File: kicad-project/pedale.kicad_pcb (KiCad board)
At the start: 2 copper layers, 118 x 73 mm, 32 parts, among them IC1 TLV76150DCYR, IC2 TLV76150DCYR, IC3 TLV76150DCYR, IC4 TLV76150DCYR, IC5 TLV76150DCYR

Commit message: Fixed 3 drc errors
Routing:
- net Net-(J14-pta8): track 30.9 -> 32.4 mm
- net Net-(J14-pta13): track 23.8 -> 25.3 mm
- net Net-(J14-pta9): track 38.1 -> 39.5 mm

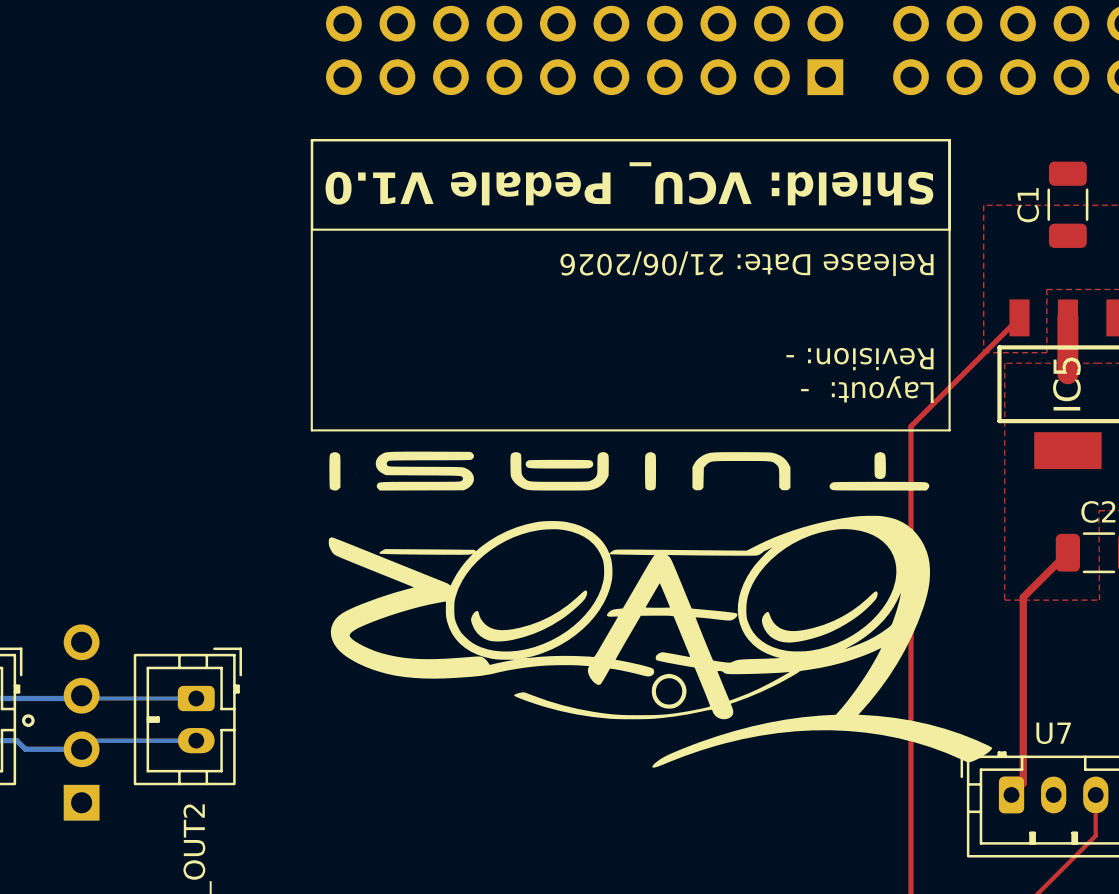
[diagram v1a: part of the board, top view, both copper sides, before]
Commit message: Fix one DRC warning for silkscreen
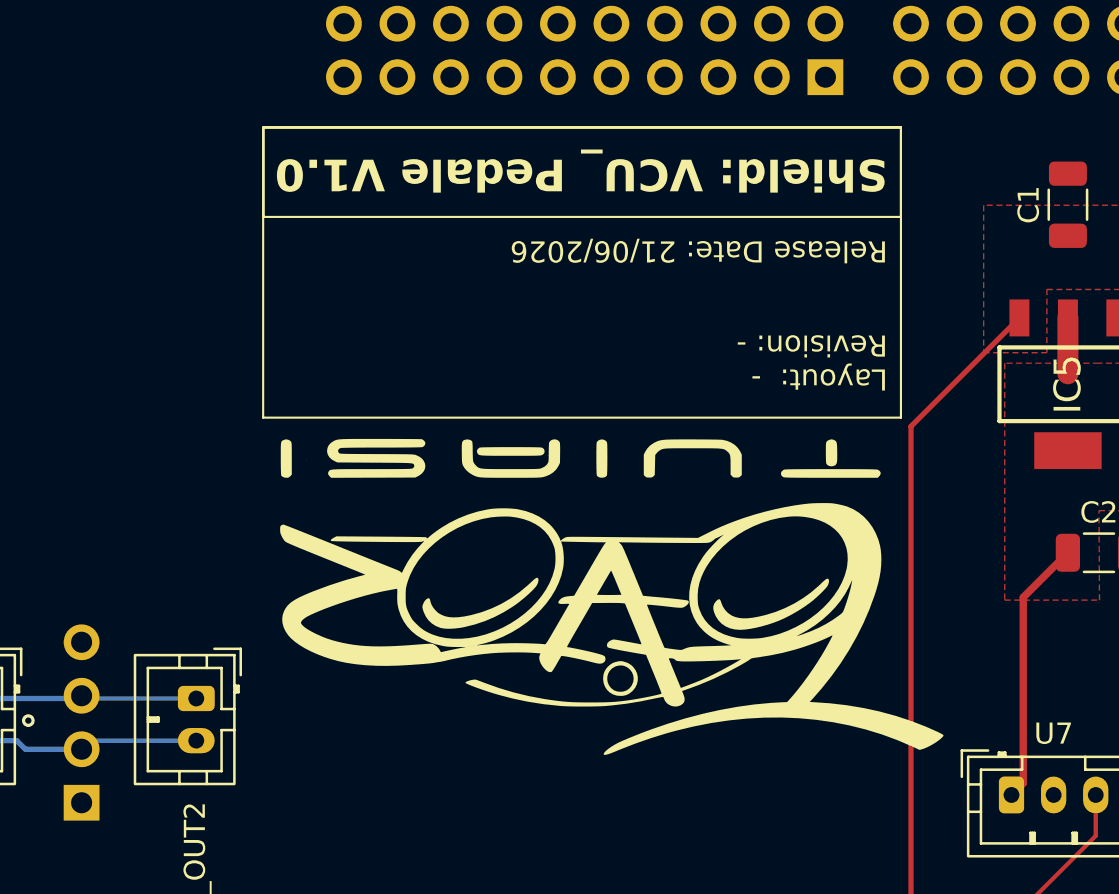
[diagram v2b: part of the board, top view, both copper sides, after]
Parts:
- moved G*** 2.39 mm to (56.5, 61.9)
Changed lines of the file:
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@@
 	(footprint "LOGO"
 		(layer "F.Cu")
-		(at 58.76 62.48 180)
+		(at 56.45 61.875 180)
 		(property "Reference" "G***"
 			(at 0 0 0)
@@
 		)
 		(property "Value" "1μF"
-			(at -0.1 -3.5 90)
+			(at -0.070001 -3.56 90)
 			(layer "F.Fab")
 			(effects
@@
 	(gr_poly
 		(pts
-			(xy 72.491955 40.19) (xy 72.491956 53.970001) (xy 42.21 53.970001) (xy 42.21 40.19)
+			(xy 70.181955 39.585) (xy 70.181956 53.365001) (xy 39.9 53.365001) (xy 39.9 39.585)
 		)
 		(stroke
@@
 	)
 	(gr_rect
-		(start 42.228045 40.19)
-		(end 72.491955 44.44)
+		(start 39.918045 39.585)
+		(end 70.181955 43.835)
 		(stroke
 			(width 0.1)
@@
 	)
 	(gr_text "Release Date: 21/06/2026"
-		(at 71.865158 45.48 180)
+		(at 69.555158 44.875 180)
 		(layer "F.SilkS")
 		(effects
@@
 	)
 	(gr_text "Layout:  -\nRevision: -"
-		(at 71.865159 49.95 180)
+		(at 69.555159 49.345 180)
 		(layer "F.SilkS")
 		(effects
@@
 	)
 	(gr_text "Shield: VCU_ Pedale V1.0"
-		(at 71.865159 41.54 180)
+		(at 69.555159 40.935 180)
 		(layer "F.SilkS")
 		(effects

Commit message: GBR added
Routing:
- net /CAN_P: track 10.5 -> 12.0 mm
- net /CAN_N: track 11.1 -> 12.4 mm
- net GND: vias 2 -> 1
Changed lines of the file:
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@@
 			(usegerberextensions no)
 			(usegerberattributes yes)
-			(usegerberadvancedattributes yes)
-			(creategerberjobfile yes)
+			(usegerberadvancedattributes no)
+			(creategerberjobfile no)
 			(dashed_line_dash_ratio 12)
 			(dashed_line_gap_ratio 3)
@@
 			(outputformat 1)
 			(mirror no)
-			(drillshape 1)
+			(drillshape 0)
 			(scaleselection 1)
-			(outputdirectory "")
+			(outputdirectory "GBR_29062026/")
 		)
 	)
@@
 	)
 	(via
-		(at 28.75 67.75)
-		(size 0.6)
-		(drill 0.3)
-		(layers "F.Cu" "B.Cu")
-		(free yes)
-		(capping no)
-		(covering
-			(front no)
-			(back no)
-		)
-		(plugging
-			(front no)
-			(back no)
-		)
-		(filling no)
-		(net "GND")
-	)
-	(via
 		(at 116.79 41.53)
 		(size 1.2)
@@
 	)
 	(segment
-		(start 31.410001 66.700001)
-		(end 31.28 66.57)
+		(start 35.855001 67.57)
+		(end 32.28 67.57)
 		(width 0.2)
 		(layer "B.Cu")
@@
 	(segment
 		(start 36.725 66.700001)
-		(end 31.410001 66.700001)
+		(end 35.855001 67.57)
 		(width 0.2)
 		(layer "B.Cu")
@@
 	)
 	(segment
-		(start 31.15 66.7)
-		(end 26.3 66.7)
-		(width 0.25)
+		(start 32.28 67.57)
+		(end 31.28 66.57)
+		(width 0.2)
 		(layer "B.Cu")
 		(net "/CAN_P")
@@
 	(segment
 		(start 31.28 66.57)
-		(end 31.15 66.7)
-		(width 0.25)
+		(end 31.13 66.57)
+		(width 0.2)
 		(layer "B.Cu")
 		(net "/CAN_P")
 	)
 	(segment
-		(start 36.725 68.700002)
-		(end 31.689998 68.700002)
+		(start 30.13 67.57)
+		(end 27.17 67.57)
 		(width 0.2)
 		(layer "B.Cu")
-		(net "/CAN_N")
+		(net "/CAN_P")
 	)
 	(segment
-		(start 28.2 68.7)
-		(end 26.3 68.7)
-		(width 0.25)
+		(start 27.17 67.57)
+		(end 26.3 66.7)
+		(width 0.2)
+		(layer "B.Cu")
+		(net "/CAN_P")
+	)
+	(segment
+		(start 31.13 66.57)
+		(end 30.13 67.57)
+		(width 0.2)
+		(layer "B.Cu")
+		(net "/CAN_P")
+	)
+	(segment
+		(start 35.8 67.97)
+		(end 32.3 67.97)
+		(width 0.2)
 		(layer "B.Cu")
 		(net "/CAN_N")
@@
 	)
 	(segment
+		(start 27.25 67.97)
+		(end 26.52 68.7)
+		(width 0.2)
+		(layer "B.Cu")
+		(net "/CAN_N")
+	)
+	(segment
 		(start 26.3 68.7)
 		(end 26.3 68.975)
@@
 	)
 	(segment
-		(start 28.61 69.11)
-		(end 28.2 68.7)
-		(width 0.25)
+		(start 31.28 68.99)
+		(end 31.28 69.11)
+		(width 0.2)
 		(layer "B.Cu")
 		(net "/CAN_N")
@@
 	(segment
 		(start 31.28 69.11)
-		(end 28.61 69.11)
-		(width 0.25)
+		(end 30.14 67.97)
+		(width 0.2)
 		(layer "B.Cu")
 		(net "/CAN_N")
 	)
 	(segment
-		(start 31.689998 68.700002)
-		(end 31.28 69.11)
+		(start 26.52 68.7)
+		(end 26.3 68.7)
+		(width 0.2)
+		(layer "B.Cu")
+		(net "/CAN_N")
+	)
+	(segment
+		(start 32.3 67.97)
+		(end 31.28 68.99)
+		(width 0.2)
+		(layer "B.Cu")
+		(net "/CAN_N")
+	)
+	(segment
+		(start 30.14 67.97)
+		(end 27.25 67.97)
+		(width 0.2)
+		(layer "B.Cu")
+		(net "/CAN_N")
+	)
+	(segment
+		(start 36.725 68.700002)
+		(end 36.530002 68.700002)
+		(width 0.2)
+		(layer "B.Cu")
+		(net "/CAN_N")
+	)
+	(segment
+		(start 36.530002 68.700002)
+		(end 35.8 67.97)
 		(width 0.2)
 		(layer "B.Cu")
@@
 		(hatch edge 0.5)
 		(priority 1)
-		(connect_pads
+		(connect_pads yes
 			(clearance 0.5)
 		)
@@
 			(thermal_gap 0.5)
 			(thermal_bridge_width 0.5)
+			(smoothing fillet)
+			(radius 2)
 			(island_removal_mode 0)
 		)
@@
 		(hatch edge 0.5)
 		(priority 2)
-		(connect_pads
+		(connect_pads yes
 			(clearance 0.5)
 		)
@@
 	)
 	(zone
-		(layers "F.Cu" "B.Cu")
-		(name "Supply GND")
-		(hatch edge 0.5)
-		(connect_pads
-			(clearance 0)
-		)
-		(min_thickness 0.25)
-		(keepout
-			(tracks allowed)
-			(vias allowed)
-			(pads allowed)
-			(copperpour not_allowed)
-			(footprints allowed)
-		)
-		(placement
-			(enabled no)
-			(sheetname "/")
-		)
-		(fill
-			(thermal_gap 0.5)
-			(thermal_bridge_width 0.5)
-			(island_removal_mode 0)
-		)
-		(polygon
-			(pts
-				(xy 123.38 40.8) (xy 123.42 43.9) (xy 128.141311 43.872342) (xy 128.123253 40.789744)
-			)
-		)
-	)
-	(zone
-		(layers "F.Cu" "B.Cu")
-		(name "Supply GND")
-		(hatch edge 0.5)
-		(connect_pads
-			(clearance 0)
-		)
-		(min_thickness 0.25)
-		(keepout
-			(tracks allowed)
-			(vias allowed)
-			(pads allowed)
-			(copperpour not_allowed)
-			(footprints allowed)
-		)
-		(placement
-			(enabled no)
-			(sheetname "/")
-		)
-		(fill
-			(thermal_gap 0.5)
-			(thermal_bridge_width 0.5)
-			(island_removal_mode 0)
-		)
-		(polygon
-			(pts
-				(xy 117.949578 39.654812) (xy 117.997391 43.360265) (xy 121.485047 43.339835) (xy 121.463414 39.647214)
-			)
-		)
-	)
-	(zone
-		(layers "F.Cu" "B.Cu")
-		(name "Supply GND")
-		(hatch edge 0.5)
-		(connect_pads
-			(clearance 0)
-		)
-		(min_thickness 0.25)
-		(keepout
-			(tracks allowed)
-			(vias allowed)
-			(pads allowed)
-			(copperpour not_allowed)
-			(footprints allowed)
-		)
-		(placement
-			(enabled no)
-			(sheetname "/")
-		)
-		(fill
-			(thermal_gap 0.5)
-			(thermal_bridge_width 0.5)
-			(island_removal_mode 0)
-		)
-		(polygon
-			(pts
-				(xy 121.014025 40.703808) (xy 121.034753 42.310194) (xy 123.504661 42.295726) (xy 123.495303 40.698443)
-			)
-		)
-	)
-	(zone
 		(net "GND")
 		(layer "B.Cu")
 		(hatch edge 0.5)
-		(connect_pads
+		(connect_pads yes
 			(clearance 0.5)
 		)
@@
 			(thermal_gap 0.5)
 			(thermal_bridge_width 0.5)
+			(smoothing fillet)
+			(radius 2)
 			(island_removal_mode 0)
 		)
